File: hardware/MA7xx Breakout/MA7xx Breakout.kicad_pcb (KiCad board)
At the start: 2 copper layers, 23 x 23 mm, 12 parts, among them IC1 MA702GQ-P, U2 MIC5504-3.3YM5

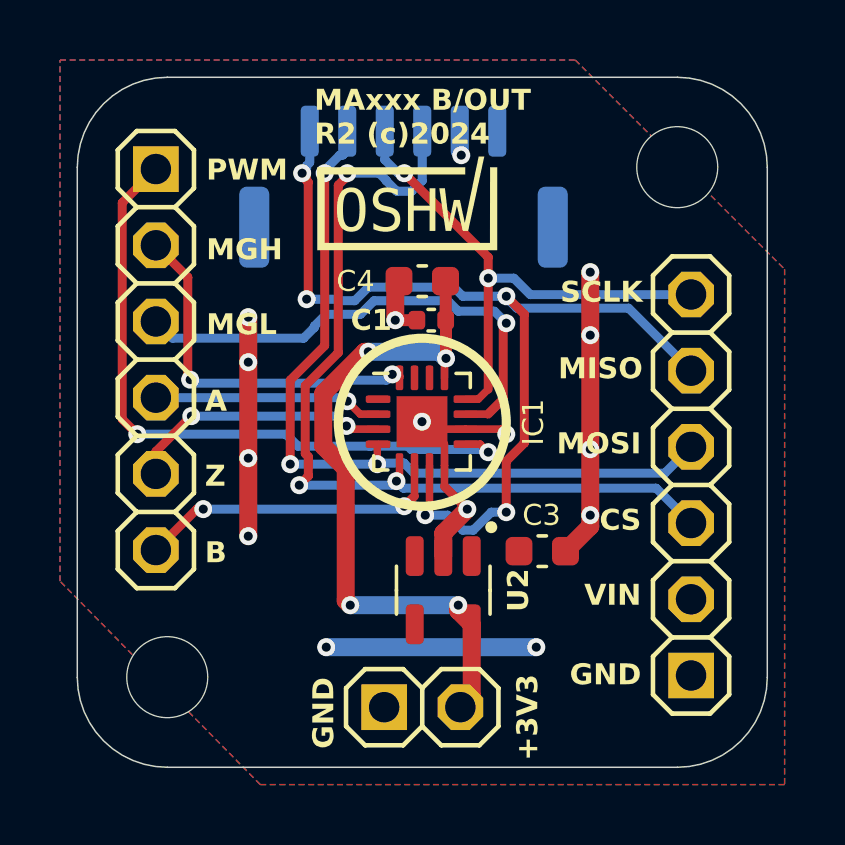
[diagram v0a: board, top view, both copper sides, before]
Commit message: update to R2.1
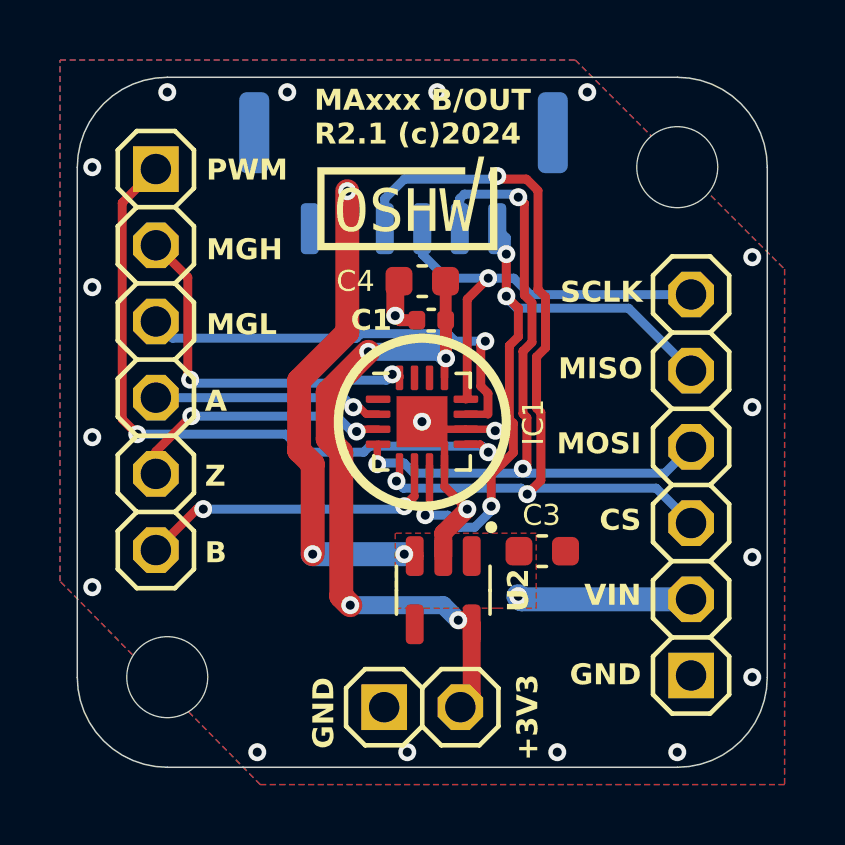
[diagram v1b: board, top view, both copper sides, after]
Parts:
- moved FLEX1 0.45 mm to (147.9, 96.7), turned to 0 degrees
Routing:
- net GND: track 27.4 -> 9.99 mm, vias 12 -> 20
- net +5V: track 7.00 -> 23.4 mm, vias 3 -> 4
- net /MISO: track 32.6 -> 21.7 mm, vias 5 -> 4
- net /SCLK: track 18.0 -> 14.7 mm, vias 2 -> 1
- net /MOSI: track 26.5 -> 24.3 mm
- net /MGL: track 16.8 -> 14.7 mm
- net /CS: track 29.4 -> 27.8 mm
- added copper zone on F.Cu, net GND
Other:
- board text added: "AYG: MA702 BKA: MA330 BRR: MA600"
- board text added: "MAxxx B/OUT R2.1 (c)2024"
- board text removed: "AYG: MA702 BKA: MA330"
- board text removed: "MAxxx B/OUT R2 (c)2024"
